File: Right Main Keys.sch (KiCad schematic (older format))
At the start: 7 parts, among them U12 SN74LVC1G04DBVR, U13 74LS597, U14 74LS597, U15 74LS597

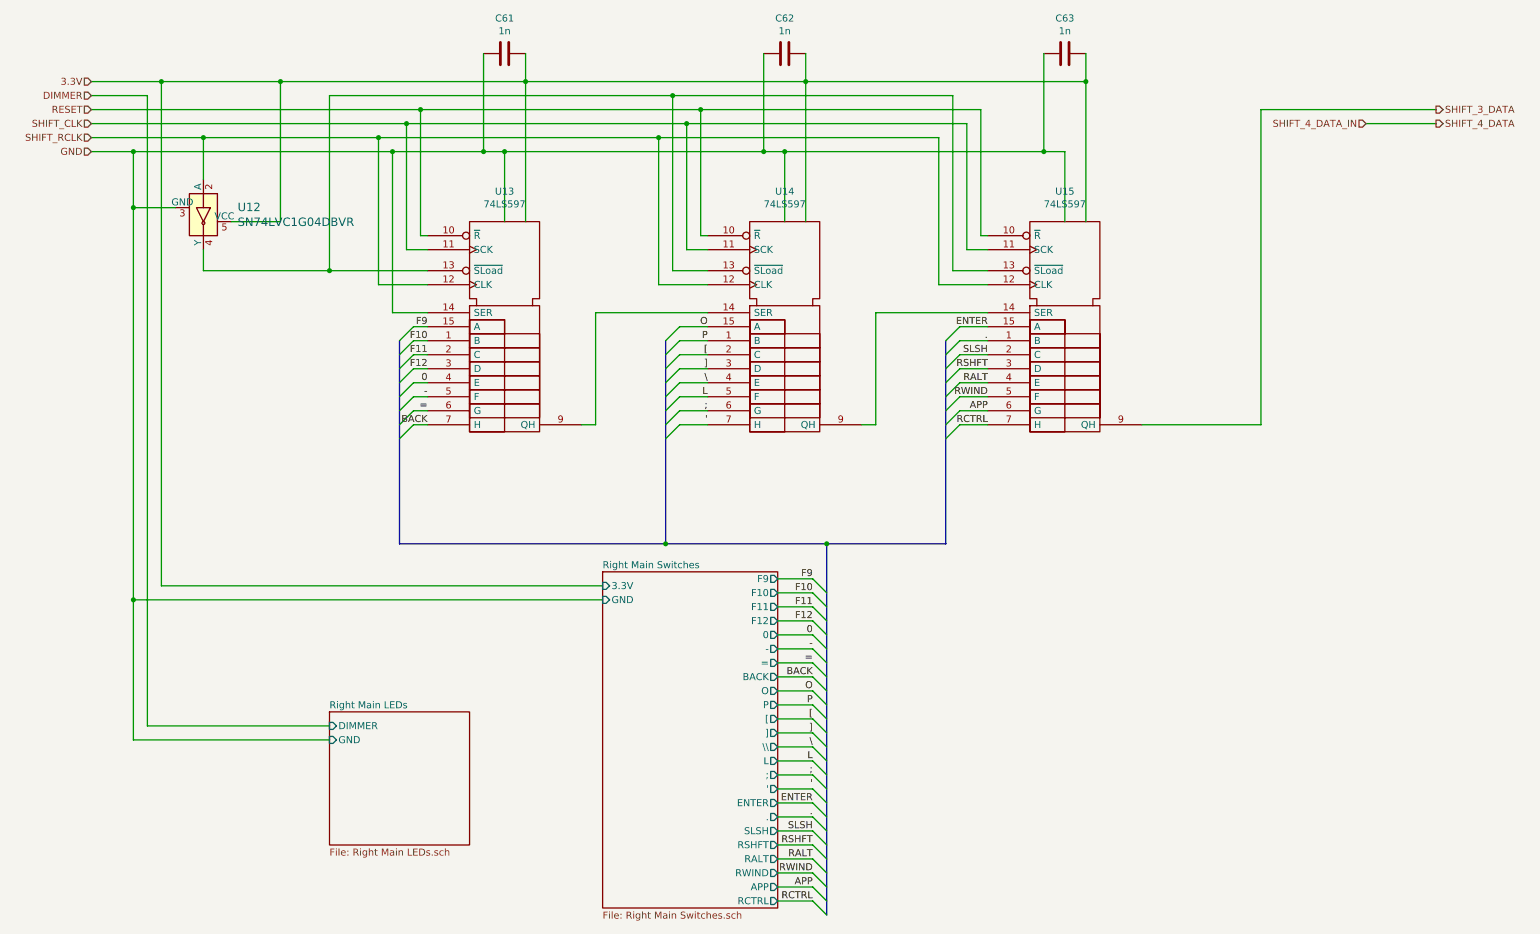
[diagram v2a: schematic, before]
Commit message: Redesigned for single large PCB
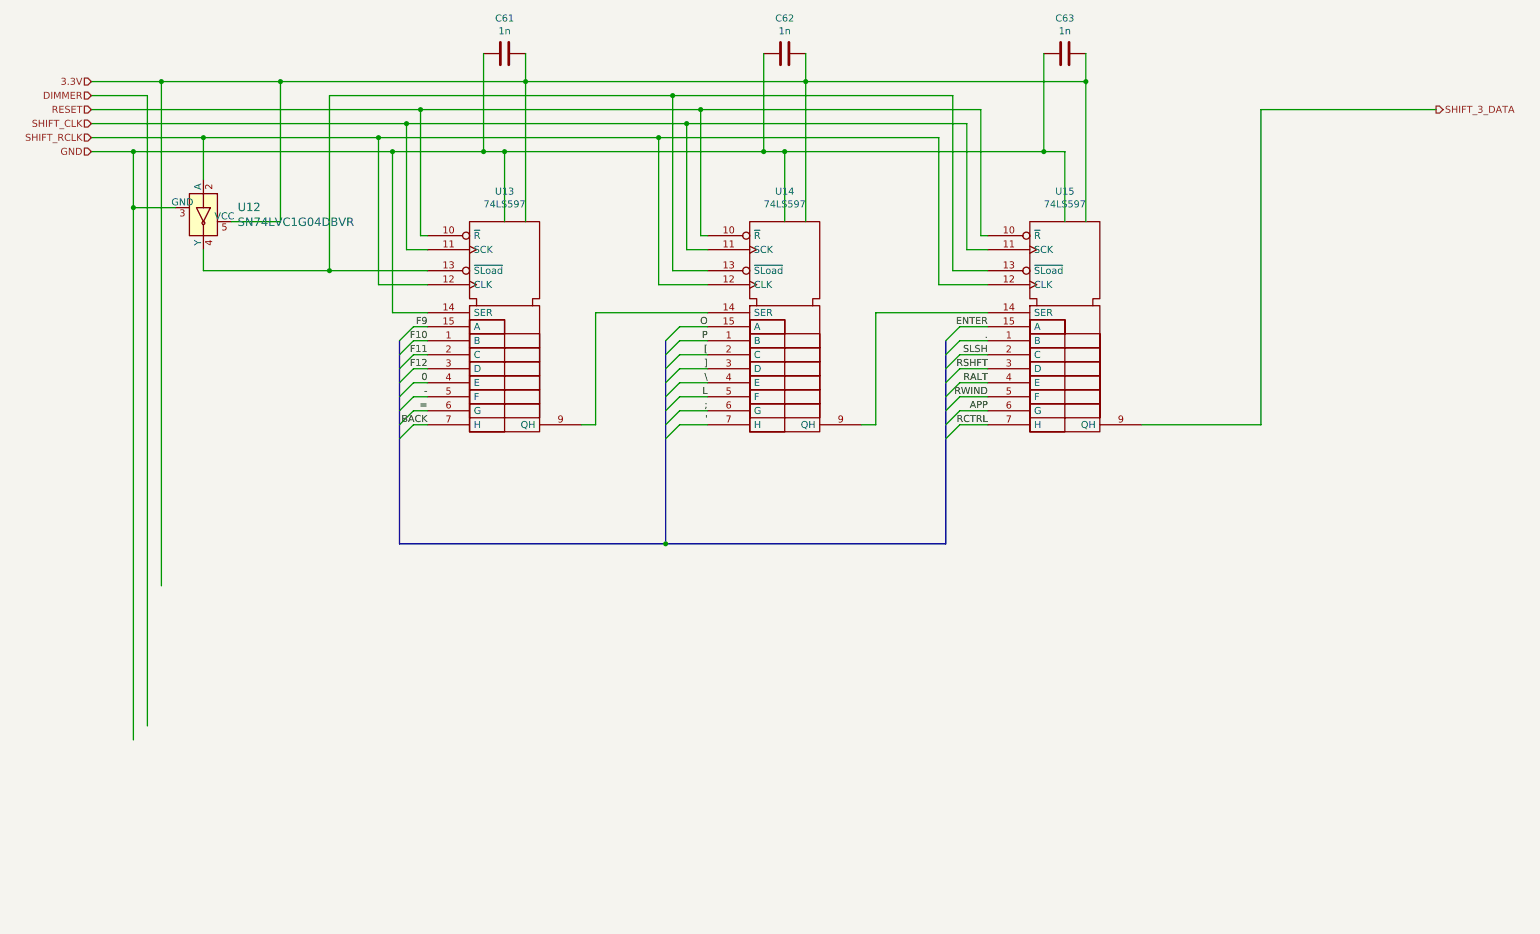
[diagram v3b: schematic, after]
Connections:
- net labels removed: SHIFT_4_DATA, SHIFT_4_DATA_IN
- wire segments 137 -> 107
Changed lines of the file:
@@
 $Descr A4 11693 8268
 encoding utf-8
-Sheet 10 18
+Sheet 14 18
 Title ""
 Date ""
@@
 Text HLabel 1000 1600 0    50   Input ~ 0
 GND
-Text HLabel 10600 1400 2    50   Output ~ 0
-SHIFT_4_DATA
 Text HLabel 10600 1300 2    50   Output ~ 0
 SHIFT_3_DATA
@@
 Wire Wire Line
 	9350 1300 10600 1300
-Entry Wire Line
-	6150 4650 6250 4750
-Text Label 6150 4650 2    50   ~ 0
-F9
-Text Label 6150 4750 2    50   ~ 0
-F10
-Text Label 6150 4850 2    50   ~ 0
-F11
-Text Label 6150 4950 2    50   ~ 0
-F12
-Text Label 6150 5050 2    50   ~ 0
-0
-Text Label 6150 5150 2    50   ~ 0
--
-Text Label 6150 5250 2    50   ~ 0
-=
-Text Label 6150 5350 2    50   ~ 0
-BACK
-Text Label 6150 5450 2    50   ~ 0
-O
-Text Label 6150 5550 2    50   ~ 0
-P
-Text Label 6150 5650 2    50   ~ 0
-[
-Text Label 6150 5750 2    50   ~ 0
-]
-Text Label 6150 5850 2    50   ~ 0
-\
-Text Label 6150 5950 2    50   ~ 0
-L
-Text Label 6150 6050 2    50   ~ 0
-;
-Text Label 6150 6150 2    50   ~ 0
-'
-Text Label 6150 6250 2    50   ~ 0
-ENTER
-Text Label 6150 6350 2    50   ~ 0
-.
-Text Label 6150 6450 2    50   ~ 0
-SLSH
-Text Label 6150 6550 2    50   ~ 0
-RSHFT
-Entry Wire Line
-	6150 4750 6250 4850
-Entry Wire Line
-	6150 4850 6250 4950
-Entry Wire Line
-	6150 4950 6250 5050
-Entry Wire Line
-	6150 5050 6250 5150
-Entry Wire Line
-	6150 5150 6250 5250
-Entry Wire Line
-	6150 5250 6250 5350
-Entry Wire Line
-	6150 5350 6250 5450
 Wire Wire Line
 	3400 2850 3300 2850
@@
 RSHFT
 Entry Wire Line
-	6150 5450 6250 5550
-Entry Wire Line
-	6150 5550 6250 5650
-Entry Wire Line
-	6150 5650 6250 5750
-Entry Wire Line
-	6150 5750 6250 5850
-Entry Wire Line
-	6150 5850 6250 5950
-Entry Wire Line
-	6150 5950 6250 6050
-Entry Wire Line
-	6150 6050 6250 6150
-Entry Wire Line
-	6150 6150 6250 6250
-Entry Wire Line
-	6150 6250 6250 6350
-Entry Wire Line
-	6150 6350 6250 6450
-Entry Wire Line
-	6150 6450 6250 6550
-Entry Wire Line
-	6150 6550 6250 6650
-Entry Wire Line
 	3200 2950 3300 2850
 Entry Wire Line
@@
 Entry Wire Line
 	7100 3250 7200 3150
-Text HLabel 10100 1400 0    50   Input ~ 0
-SHIFT_4_DATA_IN
-Wire Wire Line
-	10100 1400 10600 1400
 Wire Wire Line
 	1000 1200 1400 1200
@@
 	1400 1200 1400 5700
 Wire Wire Line
-	1400 5700 2700 5700
-Wire Wire Line
 	1500 1100 1500 4700
-Wire Wire Line
-	1300 5800 2700 5800
 Wire Wire Line
 	9350 1300 9350 3550
@@
 	1300 1600 1300 2000
 Wire Wire Line
-	4650 4800 1300 4800
-Connection ~ 1300 4800
-Wire Wire Line
-	1300 4800 1300 5800
-Wire Wire Line
-	5900 4650 6150 4650
-Wire Wire Line
-	5900 4750 6150 4750
-Wire Wire Line
-	5900 4850 6150 4850
-Wire Wire Line
-	5900 4950 6150 4950
-Wire Wire Line
-	5900 5050 6150 5050
-Wire Wire Line
-	5900 5150 6150 5150
-Wire Wire Line
-	5900 5250 6150 5250
-Wire Wire Line
-	5900 5350 6150 5350
-Wire Wire Line
-	5900 5450 6150 5450
-Wire Wire Line
-	5900 5550 6150 5550
-Wire Wire Line
-	5900 5650 6150 5650
-Wire Wire Line
-	5900 5750 6150 5750
-Wire Wire Line
-	5900 5850 6150 5850
-Wire Wire Line
-	5900 5950 6150 5950
-Wire Wire Line
-	5900 6050 6150 6050
-Wire Wire Line
-	5900 6150 6150 6150
-Wire Wire Line
-	5900 6250 6150 6250
-Wire Wire Line
-	5900 6350 6150 6350
-Wire Wire Line
-	5900 6450 6150 6450
-Wire Wire Line
-	5900 6550 6150 6550
-Wire Wire Line
-	1500 4700 4650 4700
-Wire Wire Line
 	7200 2850 7400 2850
 Wire Wire Line
@@
 Wire Wire Line
 	5200 3550 5400 3550
-$Sheet
-S 4650 4600 1250 2400
-U 5F4A8DAD
-F0 "Right Main Switches" 50
-F1 "Right Main Switches.sch" 50
-F2 "3.3V" I L 4650 4700 50
-F3 "GND" I L 4650 4800 50
-F4 "F9" O R 5900 4650 50
-F5 "F10" O R 5900 4750 50
-F6 "F11" O R 5900 4850 50
-F7 "F12" O R 5900 4950 50
-F8 "0" O R 5900 5050 50
-F9 "-" O R 5900 5150 50
-F10 "=" O R 5900 5250 50
-F11 "BACK" O R 5900 5350 50
-F12 "O" O R 5900 5450 50
-F13 "P" O R 5900 5550 50
-F14 "[" O R 5900 5650 50
-F15 "]" O R 5900 5750 50
-F16 "\\" O R 5900 5850 50
-F17 "L" O R 5900 5950 50
-F18 ";" O R 5900 6050 50
-F19 "'" O R 5900 6150 50
-F20 "ENTER" O R 5900 6250 50
-F21 "." O R 5900 6350 50
-F22 "SLSH" O R 5900 6450 50
-F23 "RSHFT" O R 5900 6550 50
-F24 "RALT" O R 5900 6650 50
-F25 "RWIND" O R 5900 6750 50
-F26 "APP" O R 5900 6850 50
-F27 "RCTRL" O R 5900 6950 50
-$EndSheet
 Text Label 7400 3250 2    50   ~ 0
 RALT
@@
 Wire Wire Line
 	7200 3550 7400 3550
-Wire Wire Line
-	5900 6650 6150 6650
-Wire Wire Line
-	5900 6750 6150 6750
-Wire Wire Line
-	5900 6850 6150 6850
-Wire Wire Line
-	5900 6950 6150 6950
-Entry Wire Line
-	6150 6650 6250 6750
-Entry Wire Line
-	6150 6750 6250 6850
-Entry Wire Line
-	6150 6850 6250 6950
-Entry Wire Line
-	6150 6950 6250 7050
-Text Label 6150 6650 2    50   ~ 0
-RALT
-Text Label 6150 6750 2    50   ~ 0
-RWIND
-Text Label 6150 6850 2    50   ~ 0
-APP
-Text Label 6150 6950 2    50   ~ 0
-RCTRL
-Wire Bus Line
-	6250 4400 5100 4400
 Connection ~ 5100 4400
 Wire Bus Line
 	5100 4400 3200 4400
-Wire Bus Line
-	7100 4400 6250 4400
-Connection ~ 6250 4400
-$Sheet
-S 2700 5600 1000 950
-U 5FECF693
-F0 "Right Main LEDs" 50
-F1 "Right Main LEDs.sch" 50
-F2 "DIMMER" I L 2700 5700 50
-F3 "GND" I L 2700 5800 50
-$EndSheet
 Wire Wire Line
 	3150 1600 3150 2750
@@
 Connection ~ 1300 2000
 Wire Wire Line
-	1300 2000 1300 4800
-Wire Wire Line
 	2000 2100 2350 2100
 Wire Wire Line
@@
 Wire Wire Line
 	6100 1100 6100 2100
+Wire Wire Line
+	1300 2000 1300 5800
+Wire Bus Line
+	5100 4400 7100 4400
 Wire Bus Line
 	7100 2950 7100 4400
@@
 Wire Bus Line
 	3200 2950 3200 4400
-Wire Bus Line
-	6250 4400 6250 7050
 $EndSCHEMATC
